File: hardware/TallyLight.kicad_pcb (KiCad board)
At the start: 4 copper layers, 68 x 68 mm, 179 parts, among them J1 Hanrun HY931147C, J2 USB_C_Receptacle_USB2.0, J3 Strapping, SW1 SW_Push, T2 HR051067, U10 EL357N(B)(TA)-G, U11 CJ431, U2 KSZ8851SNL, U3 SRV05-4, U4 ESP32-C3-WROOM-02, U5 AMS1117-3.3, U7 SRV05-4, U9 Si3402-B, Y1 25MHz

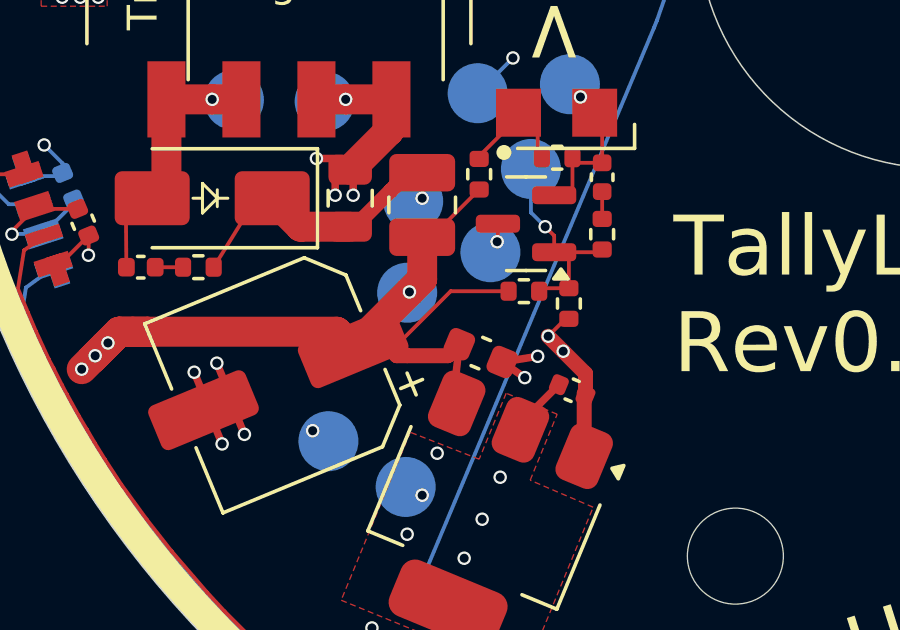
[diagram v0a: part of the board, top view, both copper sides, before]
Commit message: Optimize flyback feedback loop stability
During load testing on an initial prototype better component values for the
flyback feedback loop were found. Update design with those.
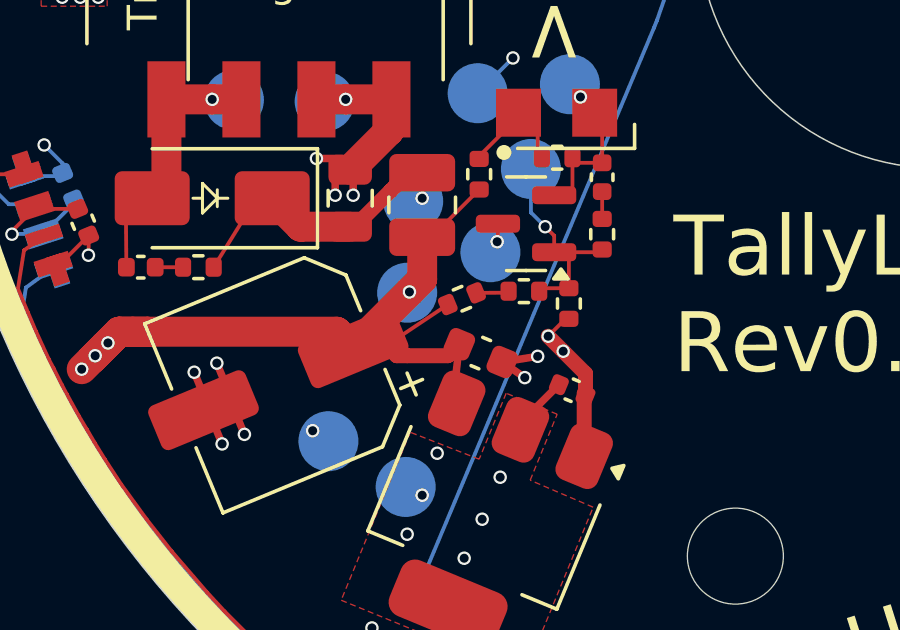
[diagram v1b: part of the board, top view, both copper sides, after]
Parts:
- added R17: 22k, Resistor_SMD:R_0402_1005Metric, F.Cu at (134.1, 112.3)
- C54: value 15nF -> 1nF
- R54: value 5.1k -> 4.7k
- R57: value 330R -> 2.2k
- R61: value 5.1k -> 33k
- TR1: value Wuerth_750315371 -> Wuerth 750315826
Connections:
- R60 pad 1: /LEDs bottom/Vled -> Net-(R17-Pad1)
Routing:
- net /LEDs bottom/Vled: track 111.8 -> 109.5 mm
- net Net-(R17-Pad1): track 0.00 -> 1.05 mm

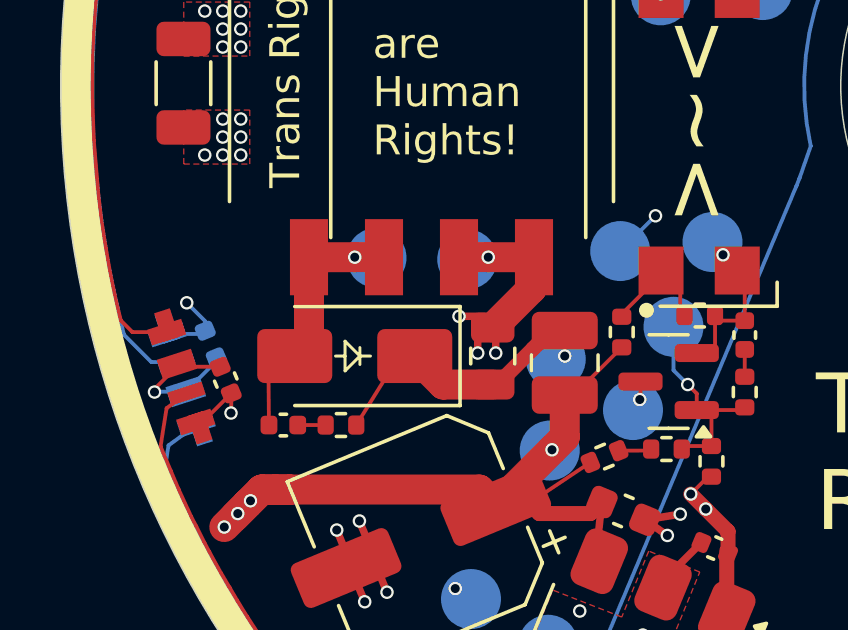
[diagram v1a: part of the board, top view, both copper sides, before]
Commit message: Improve heatsinking on secondary side flyback rectifier diode
The diode can get a bit hot under high load.
Improve its cooling.
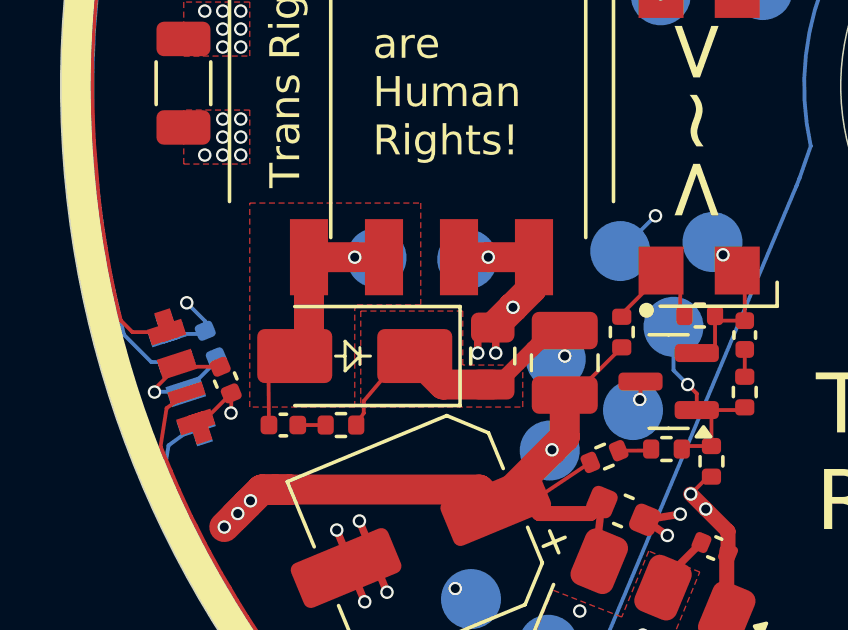
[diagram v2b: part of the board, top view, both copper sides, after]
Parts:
- R57: value 2.2k -> 1k
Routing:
- net Net-(D28-K): track 12.6 -> 13.4 mm
- net GND: track 148.7 -> 147.8 mm
- added copper zone on F.Cu, net Net-(D28-A)
- added copper zone on F.Cu, net Net-(D28-K)
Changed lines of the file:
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@@
 			)
 		)
-		(property "Value" "2.2k"
+		(property "Value" "1k"
 			(at 0 1.17 90)
 			(layer "F.Fab")
@@
 			)
 		)
-		(property "LCSC" "C25879"
+		(property "LCSC" "C11702"
 			(at 0 0 90)
 			(unlocked yes)
@@
 	)
 	(segment
-		(start 130.124997 107.675)
-		(end 129.275 107.675)
-		(width 0.25)
-		(layer "F.Cu")
-		(net 10)
-	)
-	(segment
 		(start 178.353214 104.827669)
 		(end 179.33 105.26)
@@
 	(segment
 		(start 130.4 108.050003)
-		(end 131.7 106.750003)
+		(end 131.075001 107.375002)
 		(width 1)
 		(layer "F.Cu")
@@
 	)
 	(segment
+		(start 131.075002 107.375001)
+		(end 131.7 106.750003)
+		(width 1)
+		(layer "F.Cu")
+		(net 10)
+	)
+	(segment
 		(start 170.523049 94.178361)
 		(end 171.85 94.75)
@@
 	)
 	(segment
+		(start 131.075002 107.375002)
+		(end 131.075002 107.375001)
+		(width 1)
+		(layer "F.Cu")
+		(net 10)
+	)
+	(segment
 		(start 172.998472 93.918374)
 		(end 172.45 95.15)
@@
 	)
 	(segment
+		(start 131.075001 107.375002)
+		(end 131.075002 107.375002)
+		(width 1)
+		(layer "F.Cu")
+		(net 10)
+	)
+	(segment
 		(start 174.85 95.5)
 		(end 173.95 95.45)
@@
 	)
 	(via
-		(at 129.275 107.675)
-		(size 0.45)
-		(drill 0.3)
-		(layers "F.Cu" "B.Cu")
-		(net 10)
-	)
-	(via
 		(at 145.2 74.2)
 		(size 0.45)
@@
 	)
 	(via
+		(at 131.075002 107.375002)
+		(size 0.45)
+		(drill 0.3)
+		(layers "F.Cu" "B.Cu")
+		(net 10)
+	)
+	(via
 		(at 172.125 105.25)
 		(size 0.45)
@@
 	(segment
 		(start 125.850001 111.3)
-		(end 127.075 109.325)
+		(end 126.1 110.9)
+		(width 0.127)
+		(layer "F.Cu")
+		(net 17)
+	)
+	(segment
+		(start 126.1 110.5)
+		(end 127.2 109.2)
+		(width 0.127)
+		(layer "F.Cu")
+		(net 17)
+	)
+	(segment
+		(start 127.2 109.2)
+		(end 127.8 109)
 		(width 0.127)
 		(layer "F.Cu")
@@
 		(net 17)
 	)
+	(segment
+		(start 126.1 110.9)
+		(end 126.1 110.5)
+		(width 0.127)
+		(layer "F.Cu")
+		(net 17)
+	)
 	(via
 		(at 132.8 109)
@@
 	)
 	(zone
+		(net 17)
+		(net_name "Net-(D28-K)")
+		(layer "F.Cu")
+		(hatch edge 0.5)
+		(priority 10)
+		(connect_pads yes
+			(clearance 0.1)
+		)
+		(min_thickness 0.1)
+		(filled_areas_thickness no)
+		(fill yes
+			(thermal_gap 0.5)
+			(thermal_bridge_width 0.5)
+		)
+		(polygon
+			(pts
+				(xy 126 107.5) (xy 126 110.7) (xy 131.4 110.7) (xy 131.4 109.3) (xy 129.4 109.3) (xy 129.4 107.5)
+			)
+		)
+	)
+	(zone
+		(net 8)
+		(net_name "Net-(D28-A)")
+		(layer "F.Cu")
+		(hatch edge 0.5)
+		(priority 10)
+		(connect_pads yes
+			(clearance 0.127)
+		)
+		(min_thickness 0.127)
+		(filled_areas_thickness no)
+		(fill yes
+			(thermal_gap 0.5)
+			(thermal_bridge_width 0.5)
+		)
+		(polygon
+			(pts
+				(xy 128 107.3) (xy 125.8 107.3) (xy 125.8 110.7) (xy 122.3 110.7) (xy 122.3 103.9) (xy 128 103.9)
+			)
+		)
+	)
+	(zone

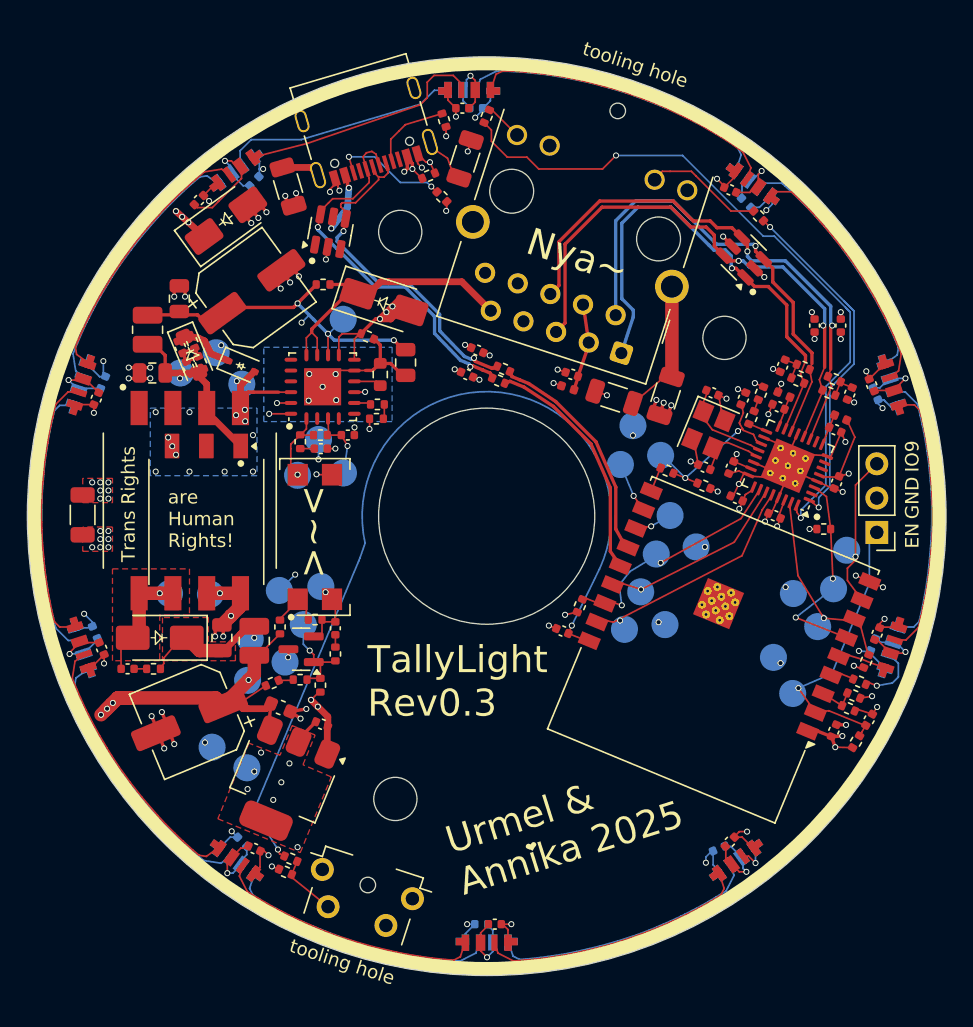
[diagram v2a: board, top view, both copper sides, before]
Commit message: rev 0.4 move button next to ethernet jack, kicad v9
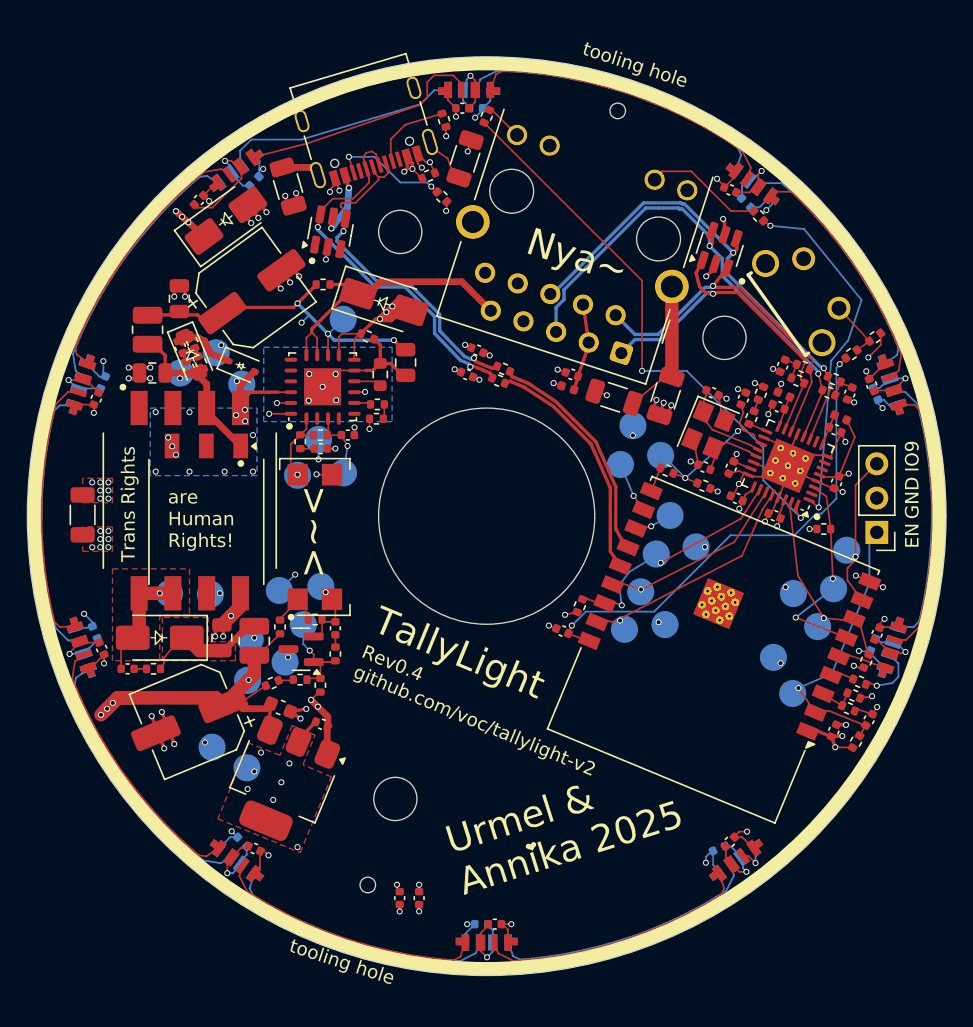
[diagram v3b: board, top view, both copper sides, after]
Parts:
- SW1: footprint Button_Switch_SMD_LCSC:x-1825027-x -> Button_Switch_SMD_LCSC_Shorter:KEY-TH_4P-L7.5-W6.8-P4.50-LS7.2
- moved R28 58.9 mm to (178.8, 86.8), turned to -144.5 degrees
- moved SW1 56.9 mm to (173.8, 83.5), turned to 125.5 degrees
- moved R16 55.8 mm to (177.0, 88.0), turned to -144.5 degrees
- moved C22 52.6 mm to (145.0, 128.3)
- moved C23 52.3 mm to (143.6, 128.3)
- moved U3 1.87 mm to (167.2, 80.2), turned to 72 degrees
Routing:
- net /Logic/LED1: track 52.8 -> 41.9 mm
- net /Logic/MDI_TX-: track 36.5 -> 26.5 mm
- net /Logic/MDI_TX+: track 35.2 -> 26.3 mm
- net /Logic/BUTTON: track 32.0 -> 35.9 mm
- net /Logic/MDI_RX-: track 40.8 -> 37.1 mm
- net /Logic/MDI_RX+: track 39.9 -> 36.5 mm
- net GND: track 147.8 -> 145.5 mm
- net +3V3: track 18.9 -> 20.6 mm
- net /LEDs bottom/Vled: track 109.5 -> 108.4 mm
- net Net-(J2-SHIELD): track 24.7 -> 24.2 mm
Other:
- board text added: "Rev0.4 github.com/voc/tallylight-v2"
- board text added: "TallyLight"
- board text removed: "TallyLight Rev0.3"

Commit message: Remove stubs from Ethernet TVS
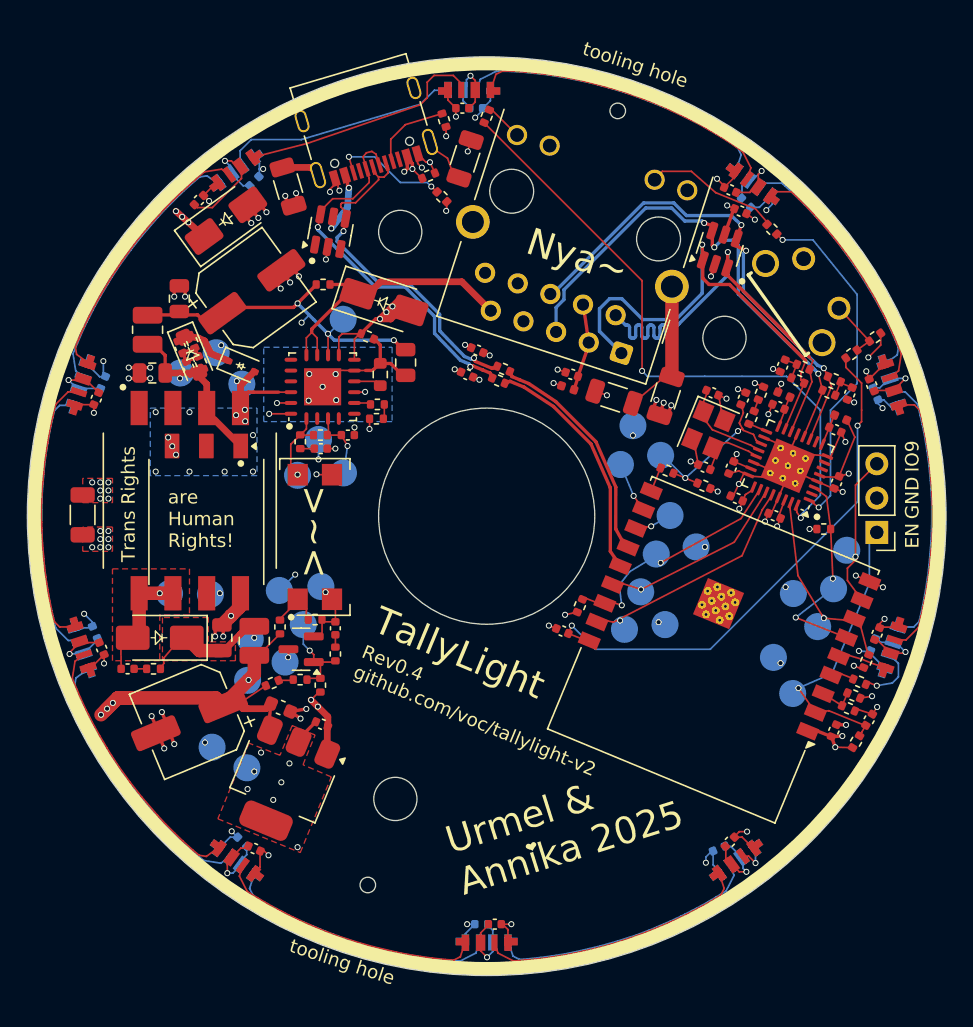
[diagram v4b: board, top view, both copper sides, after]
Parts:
- removed C23: 100nF, Capacitor_SMD:C_0402_1005Metric
- moved C22 56.1 mm to (168.8, 77.4), turned to -22.5 degrees
- moved R36 1.39 mm to (171.1, 78.8)
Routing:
- net /Logic/MDI_TX-: track 26.5 -> 35.0 mm
- net /Logic/MDI_TX+: track 26.3 -> 34.7 mm
- net /Logic/LED1: track 41.9 -> 47.2 mm
- net /Logic/BUTTON: track 35.9 -> 39.5 mm
- net Net-(J1-Pad12): track 8.83 -> 10.0 mm
- net /Logic/LED0: track 26.8 -> 25.9 mm
- net /Logic/MDI_RX-: track 37.1 -> 37.6 mm, vias 2 -> 3
- net +3V3: track 20.6 -> 21.1 mm, vias 24 -> 22
- net /Logic/MDI_RX+: track 36.5 -> 36.7 mm, vias 2 -> 3
- net GND: track 145.5 -> 145.3 mm, vias 83 -> 82
